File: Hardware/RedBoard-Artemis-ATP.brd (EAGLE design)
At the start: 101.6 x 58.4 mm, 201 parts, among them IC3 LM1117, J2 CORTEX_DEBUG, J3 POWER_JACKTOE, J5 USB-C, Q1 2.5A/30V/105mΩ, U3 AP2112-3.3V, U4 ARTEMIS_MODULESMD, U5 CH340C, Y1 32.768kHz

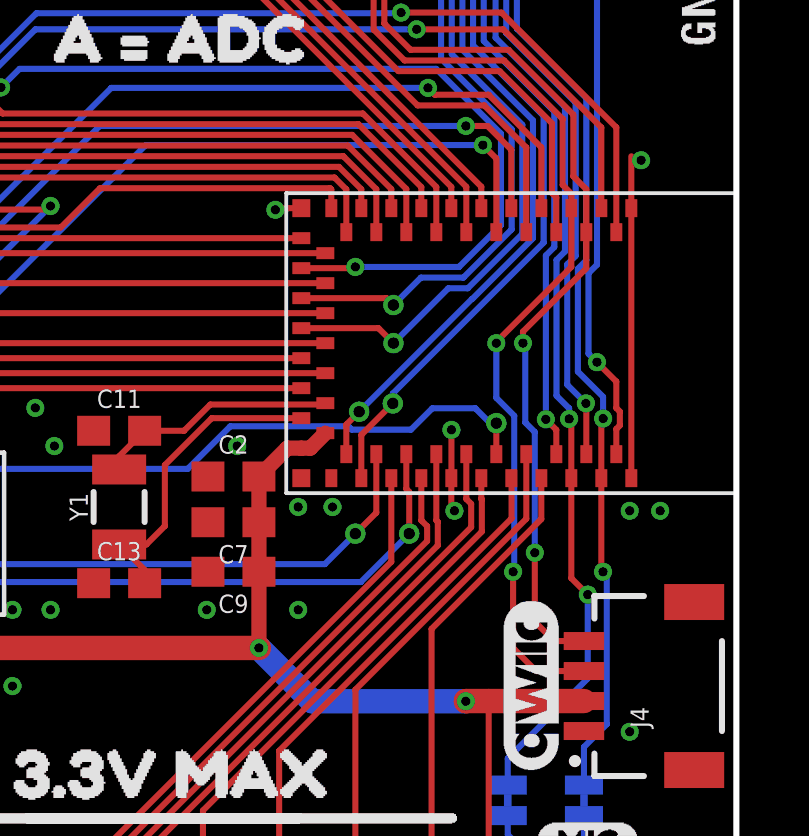
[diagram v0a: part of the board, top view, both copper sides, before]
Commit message: Adding production panels
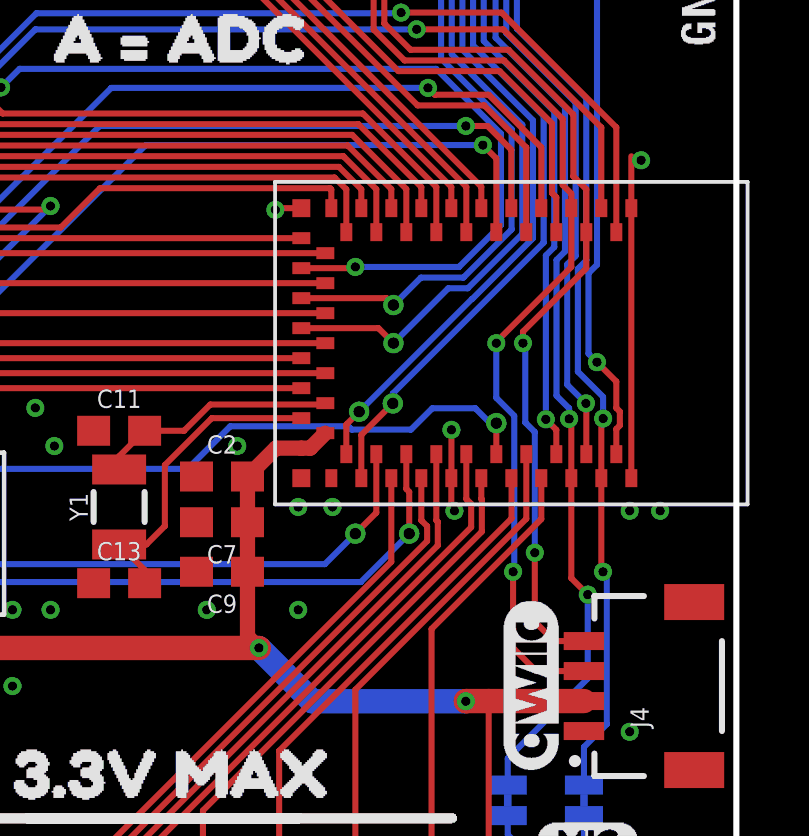
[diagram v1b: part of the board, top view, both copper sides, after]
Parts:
- U4: device Testing:ARTEMIS_FP -> SparkFun-IC-Microcontroller:ARTEMIS_FP
- moved C2 0.38 mm to (84.5, 24.8)
- moved C7 0.38 mm to (84.5, 23.2)
- moved C9 0.38 mm to (84.5, 21.6)
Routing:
- net VDD: track 176.2 -> 176.8 mm
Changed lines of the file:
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@@
 <attribute name="VALUE" value="100k" x="15.113" y="47.117" size="0.6096" layer="27" font="vector" ratio="15"/>
 </element>
-<element name="C2" library="SparkFun-Capacitors" package="0603" value="0.1uF" x="84.836" y="24.765" smashed="yes">
-<attribute name="NAME" x="84.836" y="25.527" size="0.6096" layer="25" font="vector" ratio="20" align="bottom-center"/>
-<attribute name="PROD_ID" value="CAP-00810" x="84.836" y="24.765" size="1.778" layer="27" display="off"/>
-<attribute name="VALUE" x="82.804" y="24.003" size="0.6096" layer="27" font="vector" ratio="15" rot="R180" align="top-center"/>
+<element name="C2" library="SparkFun-Capacitors" package="0603" value="0.1uF" x="84.455" y="24.765" smashed="yes">
+<attribute name="NAME" x="84.455" y="25.527" size="0.6096" layer="25" font="vector" ratio="20" align="bottom-center"/>
+<attribute name="PROD_ID" value="CAP-00810" x="84.455" y="24.765" size="1.778" layer="27" display="off"/>
+<attribute name="VALUE" x="82.423" y="24.003" size="0.6096" layer="27" font="vector" ratio="15" rot="R180" align="top-center"/>
 </element>
 <element name="C3" library="SparkFun-Capacitors" package="EIA3216" value="10uF" x="20.32" y="16.002" smashed="yes" rot="R180">
@@
 <element name="J2" library="SparkFun-Connectors" package="2X5-SMD-1.27MM" value="CORTEX_DEBUG" x="72.39" y="22.86" smashed="yes">
 <attribute name="NAME" x="70.8152" y="24.7904" size="0.6096" layer="25" font="vector" ratio="20"/>
+<attribute name="PROD_ID" value="CONN-14468" x="72.39" y="22.86" size="1.778" layer="27" display="off"/>
 <attribute name="VALUE" x="70.5612" y="20.3962" size="0.6096" layer="27" font="vector" ratio="20"/>
 </element>
@@
 <attribute name="VALUE" value="0.1uF" x="21.971" y="42.037" size="0.6096" layer="27" font="vector" ratio="20" align="top-center"/>
 </element>
-<element name="C7" library="SparkFun-Capacitors" package="0603" value="10uF" x="84.836" y="23.241" smashed="yes" rot="R180">
-<attribute name="NAME" x="84.836" y="22.479" size="0.6096" layer="25" font="vector" ratio="20" rot="R180" align="bottom-center"/>
-<attribute name="PROD_ID" value="CAP-11015" x="84.836" y="23.241" size="1.778" layer="27" font="vector" ratio="15" rot="R180" display="off"/>
-<attribute name="VALUE" x="86.995" y="22.987" size="0.6096" layer="27" font="vector" ratio="20" rot="R180" align="top-center"/>
-</element>
-<element name="C9" library="SparkFun-Capacitors" package="0603" value="1.0uF" x="84.836" y="21.59" smashed="yes" rot="R180">
-<attribute name="NAME" x="84.836" y="20.828" size="0.6096" layer="25" font="vector" ratio="20" rot="R180" align="bottom-center"/>
-<attribute name="PROD_ID" value="CAP-00868" x="84.836" y="21.59" size="1.778" layer="27" font="vector" ratio="15" rot="R180" display="off"/>
-<attribute name="VALUE" x="86.995" y="21.336" size="0.6096" layer="27" font="vector" ratio="20" rot="R180" align="top-center"/>
+<element name="C7" library="SparkFun-Capacitors" package="0603" value="10uF" x="84.455" y="23.241" smashed="yes" rot="R180">
+<attribute name="NAME" x="84.455" y="22.479" size="0.6096" layer="25" font="vector" ratio="20" rot="R180" align="bottom-center"/>
+<attribute name="PROD_ID" value="CAP-11015" x="84.455" y="23.241" size="1.778" layer="27" font="vector" ratio="15" rot="R180" display="off"/>
+<attribute name="VALUE" x="86.614" y="22.987" size="0.6096" layer="27" font="vector" ratio="20" rot="R180" align="top-center"/>
+</element>
+<element name="C9" library="SparkFun-Capacitors" package="0603" value="1.0uF" x="84.455" y="21.59" smashed="yes" rot="R180">
+<attribute name="NAME" x="84.455" y="20.828" size="0.6096" layer="25" font="vector" ratio="20" rot="R180" align="bottom-center"/>
+<attribute name="PROD_ID" value="CAP-00868" x="84.455" y="21.59" size="1.778" layer="27" font="vector" ratio="15" rot="R180" display="off"/>
+<attribute name="VALUE" x="86.614" y="21.336" size="0.6096" layer="27" font="vector" ratio="20" rot="R180" align="top-center"/>
 </element>
 <element name="TP3" library="SparkFun-Connectors" package="PAD.03X.05" value="" x="67.31" y="24.13" smashed="yes" rot="MR0"/>
@@
 <attribute name="VALUE" x="94.615" y="12.065" size="0.6" layer="27" font="vector"/>
 </element>
-<element name="U4" library="Testing" package="ARTEMIS_FP" value="ARTEMIS_MODULESMD" x="93.599" y="29.21" smashed="yes"/>
+<element name="U4" library="SparkFun-IC-Microcontroller" package="ARTEMIS_FP" value="ARTEMIS_MODULESMD" x="93.599" y="29.21" smashed="yes">
+<attribute name="PROD_ID" value="SUB-14415" x="93.599" y="29.21" size="1.778" layer="27" display="off"/>
+</element>
 <element name="U$17" library="buzzard_labels" package="A160" value="" x="60.96" y="8.001" smashed="yes" rot="R90"/>
 <element name="U$19" library="buzzard_labels (1)" package="#48" value="" x="55.88" y="47.371" smashed="yes" rot="R90"/>
@@
 <wire x1="19.096" y1="37.257" x2="19.096" y2="45.42" width="0.2032" layer="1"/>
 <wire x1="30.48" y1="6.73" x2="30.48" y2="3.43" width="0.2032" layer="1"/>
-<wire x1="85.686" y1="23.241" x2="85.686" y2="21.59" width="0.508" layer="1"/>
-<wire x1="85.686" y1="24.765" x2="85.686" y2="23.241" width="0.508" layer="1"/>
-<wire x1="85.686" y1="19.05" x2="85.686" y2="21.59" width="0.508" layer="1"/>
+<wire x1="85.305" y1="23.241" x2="85.305" y2="21.59" width="0.508" layer="1"/>
+<wire x1="85.305" y1="24.765" x2="85.305" y2="23.241" width="0.508" layer="1"/>
+<wire x1="85.305" y1="21.59" x2="85.305" y2="19.431" width="0.508" layer="1"/>
+<wire x1="85.686" y1="19.05" x2="85.305" y2="19.431" width="0.508" layer="1"/>
 <wire x1="19.096" y1="45.42" x2="17.399" y2="47.117" width="0.2032" layer="1"/>
 <wire x1="15.152" y1="47.586" x2="15.152" y2="48.26" width="0.2032" layer="1"/>
@@
 <contactref element="U4" pad="VDD@36"/>
 <contactref element="U4" pad="VDD@37"/>
-<wire x1="87.099" y1="25.71" x2="86.631" y2="25.71" width="0.508" layer="1"/>
-<wire x1="85.686" y1="24.765" x2="86.631" y2="25.71" width="0.508" layer="1"/>
+<wire x1="87.099" y1="25.71" x2="86.25" y2="25.71" width="0.508" layer="1"/>
+<wire x1="85.305" y1="24.765" x2="86.25" y2="25.71" width="0.508" layer="1"/>
 <wire x1="87.099" y1="25.71" x2="87.399" y2="25.71" width="0.508" layer="1"/>
 <wire x1="87.399" y1="25.71" x2="87.899" y2="26.21" width="0.508" layer="1"/>

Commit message: Adding designed by text
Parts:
- moved FRAME3 44.4 mm to (17.8, -8.89)
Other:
- board text added: "N. Seidle"
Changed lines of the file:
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@@
 <wire x1="40.64" y1="1.143" x2="43.053" y2="1.143" width="1.27" layer="22"/>
 <wire x1="26.289" y1="57.15" x2="23.876" y2="57.15" width="1.27" layer="22"/>
+<text x="48.26" y="-8.89" size="1.778" layer="51" font="vector" ratio="15">N. Seidle</text>
 </plain>
 <attributes>
@@
 <element name="U$116" library="buzzard_labels (2)" package="TX10" value="" x="60.96" y="56.515" smashed="yes" rot="MR270"/>
 <element name="LOGO1" library="SparkFun-Aesthetics" package="SFE_LOGO_NAME_FLAME_.1" value="SFE_LOGO_NAME_FLAME.1_INCH" x="87.503" y="35.306" smashed="yes" rot="MR0"/>
-<element name="FRAME3" library="SparkFun-Aesthetics" package="CREATIVE_COMMONS" value="FRAME-LEDGER" x="-5.08" y="-46.99" smashed="yes">
-<attribute name="DESIGNER" value="" x="-5.08" y="-46.99" size="1.778" layer="27" font="vector" ratio="15" display="off"/>
-<attribute name="REV" value="" x="-5.08" y="-46.99" size="1.778" layer="27" font="vector" ratio="15" display="off"/>
+<element name="FRAME3" library="SparkFun-Aesthetics" package="CREATIVE_COMMONS" value="FRAME-LEDGER" x="17.78" y="-8.89" smashed="yes">
+<attribute name="DESIGNER" value="" x="17.78" y="-8.89" size="1.778" layer="27" font="vector" ratio="15" display="off"/>
+<attribute name="REV" value="" x="17.78" y="-8.89" size="1.778" layer="27" font="vector" ratio="15" display="off"/>
 </element>
 <element name="JP27" library="SparkFun-Connectors" package="1X08_NO_SILK" value="" x="50.8" y="1.27" smashed="yes">
